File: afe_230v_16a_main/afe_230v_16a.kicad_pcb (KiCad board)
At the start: 2 copper layers, 342.7 x 117.6 mm, 60 parts, among them J4 MCV 1,5/ 6-G-3,81, J5 HBUS16, J6 pinheader_1x6, U2 AD8538, U3 AD8538_dnp, U4 AQH3223A, U5 ACS711xLCTR-25AB, U6 AD8538_dnp, U7 REF3030, U9 YAAJ_BlackPill

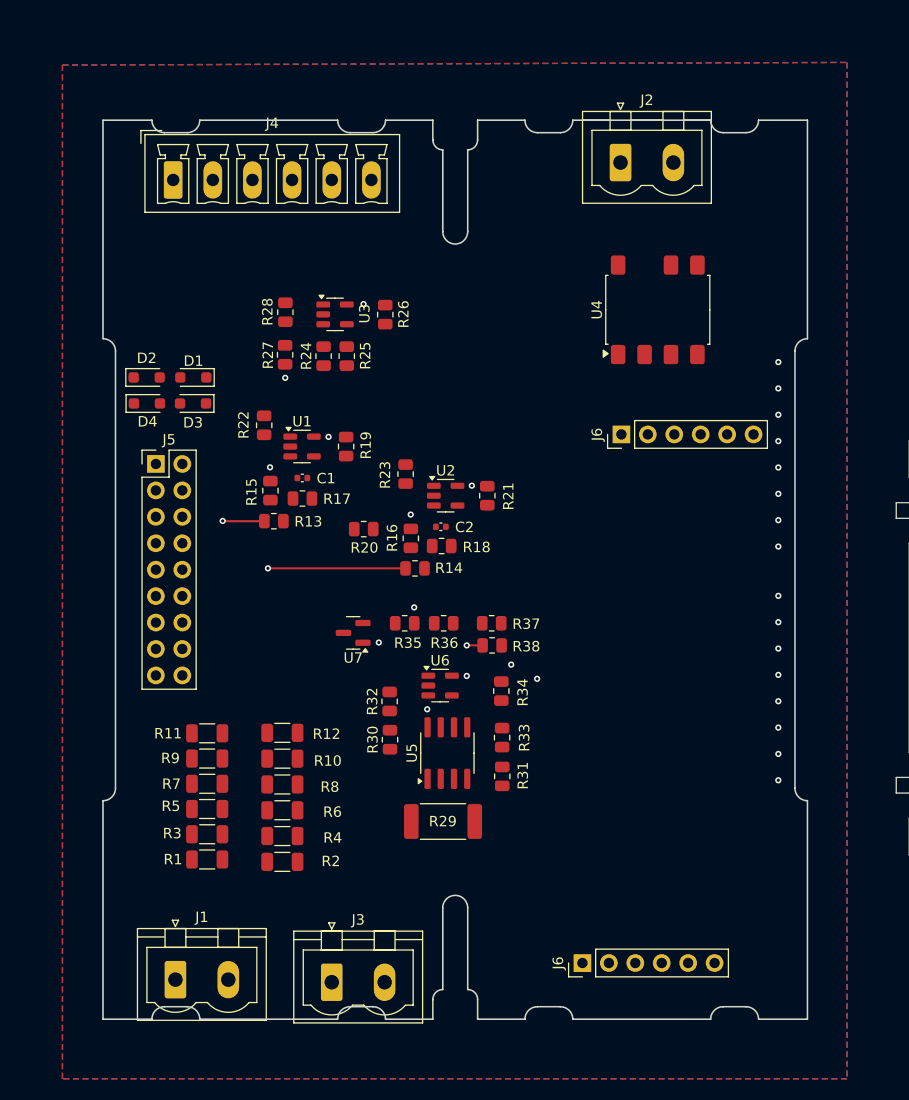
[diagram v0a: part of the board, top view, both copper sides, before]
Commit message: adjusted HBUS, DNP, & fixed A5toA2
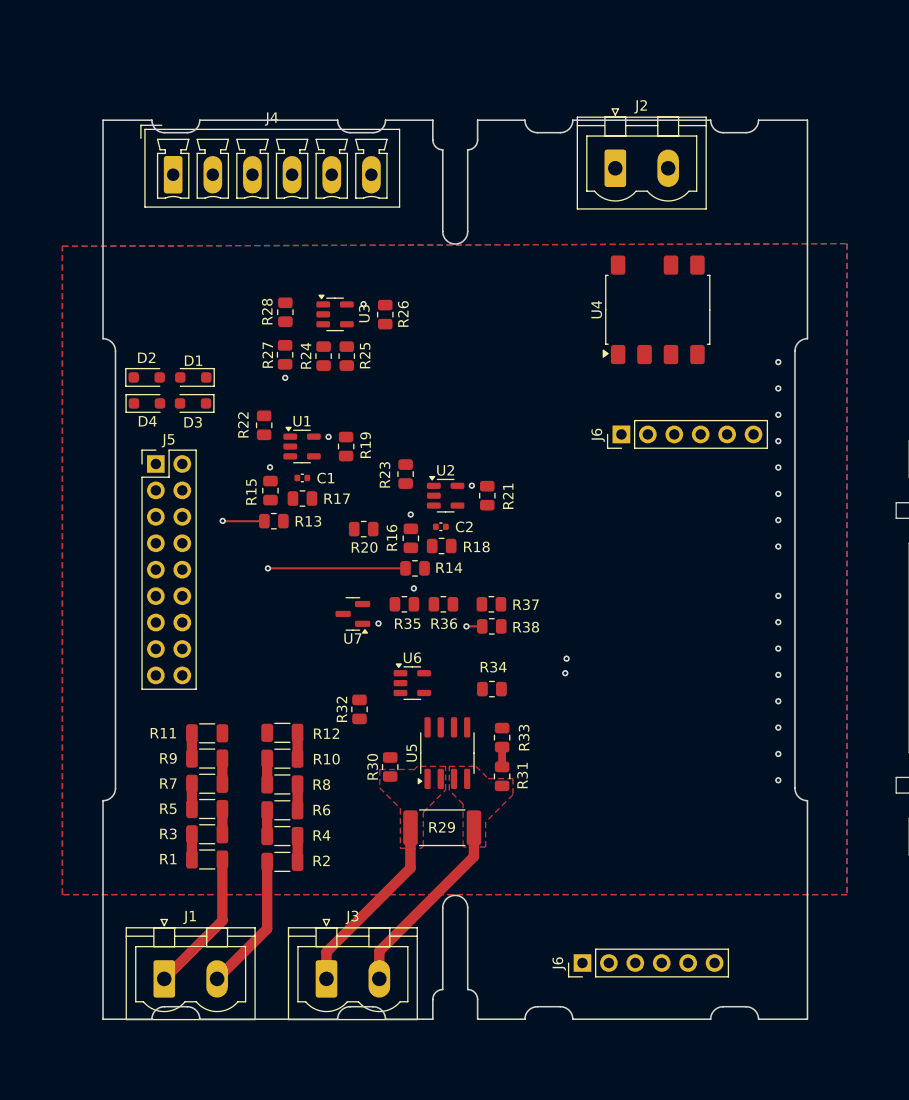
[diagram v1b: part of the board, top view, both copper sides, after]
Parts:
- moved R32 2.99 mm to (142.6, 108.1)
- moved U6 2.68 mm to (147.7, 105.5)
- moved R30 2.63 mm to (145.6, 113.6)
- moved R35 1.83 mm to (146.9, 98.0)
- moved R36 1.83 mm to (150.7, 98.0)
- moved R37 1.83 mm to (155.3, 98.0)
- moved R38 1.83 mm to (155.3, 100.1)
- moved U7 1.83 mm to (142.0, 98.9)
- moved J1 1.08 mm to (123.8, 134.0)
- moved R34 0.92 mm to (155.3, 106.1), turned to 180 degrees
- moved J2 0.74 mm to (167.2, 56.1)
- moved R29 0.61 mm to (150.6, 119.5)
- moved J3 0.60 mm to (139.4, 134.0)
- moved J4 0.50 mm to (124.7, 56.7)
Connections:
- J5 pad 1: /V0_sense -> /24V
- J5 pad 10: unconnected-(J5-Pin_10-Pad10) -> /V2_sense
- J5 pad 11: /CAN_hi -> /CAN_lo
- J5 pad 12: /K1_on -> /V3_sense
- J5 pad 13: /CAN_lo -> /I0_sense
- J5 pad 14: /K1_status -> /V4_sense
- J5 pad 15: /24V -> unconnected-(J5-Pin_15-Pad15)
- J5 pad 16: /K2_on -> unconnected-(J5-Pin_16-Pad16)
- J5 pad 17: /DGND -> unconnected-(J5-Pin_17-Pad17)
- J5 pad 18: /K2_status -> unconnected-(J5-Pin_18-Pad18)
- J5 pad 2: /V2_sense -> /K0_on
- J5 pad 3: /V1_sense -> /DGND
- J5 pad 4: /V3_sense -> /K1_on
- J5 pad 5: /K0_on -> /V0_sense
- J5 pad 6: /V4_sense -> /K0_status
- J5 pad 7: /K0_status -> /V1_sense
- J5 pad 8: /I0_sense -> /K1_status
- J5 pad 9: unconnected-(J5-Pin_9-Pad9) -> /CAN_hi
- U5 pad 7: /A5 -> /A2
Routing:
- net /I_n: track 0.00 -> 18.3 mm
- net /I_p: track 0.00 -> 17.9 mm
- net /V0_p: track 0.00 -> 13.8 mm
- net /V0_n: track 0.00 -> 13.2 mm
- net Net-(R4-Pad2): track 0.00 -> 2.48 mm
- net Net-(R2-Pad2): track 0.00 -> 2.48 mm
- net Net-(R10-Pad2): track 0.00 -> 2.48 mm
- net Net-(R10-Pad1): track 0.00 -> 2.48 mm
- net Net-(R6-Pad2): track 0.00 -> 2.48 mm
- net Net-(R5-Pad2): track 0.00 -> 2.43 mm
- net Net-(R7-Pad2): track 0.00 -> 2.42 mm
- net Net-(R3-Pad2): track 0.00 -> 2.42 mm
- net Net-(R11-Pad1): track 0.00 -> 2.42 mm
- net Net-(R1-Pad2): track 0.00 -> 2.42 mm
- net Net-(U6--): track 0.00 -> 1.90 mm
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- added copper zone on F.Cu, net /I_n
- added copper zone on F.Cu, net /I_p

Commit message: initial routing
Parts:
- moved J2 77.9 mm to (167.1, 134.0)
- moved J6 75.8 mm to (163.3, 56.6)
- moved U4 50.1 mm to (170.2, 119.8), turned to 180 degrees
- moved U6 4.70 mm to (143.4, 107.5)
- moved R32 3.68 mm to (143.4, 111.7)
- moved U7 0.52 mm to (142.0, 99.4)
- moved R34 0.15 mm to (155.4, 106.2)
- moved U5 0.09 mm to (151.0, 112.2)
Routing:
- net /3V3: track 0.00 -> 171.5 mm
- net /A2: track 0.00 -> 122.0 mm
- net /D0: track 0.00 -> 121.2 mm
- net /DGND: track 0.00 -> 103.2 mm
- net /A0: track 0.00 -> 102.4 mm, vias 0 -> 1
- net /A1: track 0.00 -> 96.9 mm, vias 0 -> 1
- net /V1_sense: track 13.2 -> 56.2 mm, vias 1 -> 2
- net /V0_sense: track 4.02 -> 45.2 mm, vias 1 -> 2
- net /1V5_REF: track 0.00 -> 39.7 mm
- net /I0_sense: track 1.53 -> 33.0 mm
- net /3V0_REF: track 0.00 -> 30.7 mm
- net Net-(R20-Pad2): track 0.00 -> 28.4 mm
- net Net-(R33-Pad2): track 0.00 -> 22.0 mm
- net /K_o: track 0.00 -> 18.5 mm
- net Net-(U6--): track 1.90 -> 16.8 mm
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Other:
- board text added: "DG 3v3 A0 A1 A2 D0"
- board text added: "I P"
- board text added: "K I"
- board text added: "K O"
- board text added: "V P"

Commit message: located daughterboard & updated connector
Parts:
- added 000: 0, Resistor_SMD:R_0805_2012Metric, F.Cu at (122.5, 72.3)
- added R39: 0, Resistor_SMD:R_0805_2012Metric, F.Cu at (1.71, 0.97)
- J6 (x2): value pinheader_1x6 -> pinheader_2x6_socket; footprint Connector_PinHeader_2.54mm:PinHeader_1x06_P2.54mm_Vertical -> Connector_PinHeader_2.54mm:PinHeader_2x06_P2.54mm_Vertical
- moved J6 4.47 mm to (245.5, 88.8)
- moved R1 2.63 mm to (125.7, 123.9), turned to 0 degrees
- moved R10 2.60 mm to (133.4, 111.0), turned to 90 degrees
- moved R12 2.58 mm to (136.0, 107.9), turned to 90 degrees
- moved J6 2.54 mm to (167.8, 84.2)
- moved R3 2.30 mm to (129.3, 121.9), turned to 90 degrees
- moved R6 1.74 mm to (133.6, 117.2), turned to 90 degrees
- moved R11 1.70 mm to (129.4, 109.5), turned to 90 degrees
- moved R5 1.59 mm to (126.9, 118.8), turned to 90 degrees
- moved U9 1.58 mm to (208.8, 113.6)
- moved R7 1.49 mm to (129.4, 115.7), turned to 90 degrees
- moved R2 1.45 mm to (134.5, 124.0)
- moved R8 1.40 mm to (136.0, 114.1), turned to 90 degrees
- moved R9 1.06 mm to (126.9, 112.6), turned to 90 degrees
- moved R4 0.88 mm to (136.1, 120.4), turned to 90 degrees
- renumbered J6 to J8
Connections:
- J6 pad 1: /DGND -> Earth (x2)
- J6 pad 2: /3V3 -> /DGND (x2)
- J6 pad 3: /A0 -> unconnected-(J6-Pin_3-Pad3) (x2)
- J6 pad 4: /A1 -> /3V3 (x2)
- J6 pad 5: /A2 -> unconnected-(J6-Pin_5-Pad5) (x2)
- J6 pad 6: /D0 -> /A0 (x2)
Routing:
- net /D0: track 121.2 -> 172.3 mm
- net /A2: track 122.0 -> 153.7 mm
- net /3V3: track 171.5 -> 202.8 mm
- net /A1: track 96.9 -> 124.0 mm
- net /A0: track 102.4 -> 125.0 mm
- net /V1_sense: track 56.2 -> 52.2 mm
- net /V0_p: track 13.8 -> 10.3 mm
- net /DGND: track 103.2 -> 106.3 mm, vias 0 -> 1
- net Net-(R4-Pad2): track 2.48 -> 0.00 mm
- net Net-(R2-Pad2): track 2.48 -> 0.00 mm
- net Net-(R10-Pad2): track 2.48 -> 0.00 mm
- net Net-(R10-Pad1): track 2.48 -> 0.00 mm
- net Net-(R6-Pad2): track 2.48 -> 0.00 mm
- net Net-(R5-Pad2): track 2.43 -> 0.00 mm
- net Net-(R7-Pad2): track 2.42 -> 0.00 mm
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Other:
- board size 342.7 x 117.6 mm -> 429.1 x 163.3 mm
- board text added: "BC 71,6 UT11/22 pcb4 13.6mm clearance"

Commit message: changed BP footprint, added stlink connection, added 3d models
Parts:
- removed U9: YAAJ_BlackPill, STM-32:YAAJ_BlackPill_SWD_2
- added C10: 0.1uF, Capacitor_SMD:C_0603_1608Metric_Pad1.08x0.95mm_HandSolder, F.Cu at (138.1, 67.5)
- added C4: 0.1uF, Capacitor_SMD:C_0603_1608Metric_Pad1.08x0.95mm_HandSolder, F.Cu at (143.6, 104.6)
- added C5: 0.1uF, Capacitor_SMD:C_0603_1608Metric_Pad1.08x0.95mm_HandSolder, F.Cu at (151.0, 83.6)
- added C6: 0.1uF, Capacitor_SMD:C_0603_1608Metric_Pad1.08x0.95mm_HandSolder, F.Cu at (136.4, 78.8)
- added J7: 1x02_pinheader, Connector_PinHeader_2.54mm:PinHeader_1x02_P2.54mm_Vertical, F.Cu at (157.8, 57.9)
- added J9: Conn_01x04_STlink_pinheader, Connector_PinHeader_2.54mm:PinHeader_1x04_P2.54mm_Vertical, F.Cu at (173.3, 132.9)
- added U10: BlackPill_F4_SWI, MSZ_STM32:Blackpill_F4_SWI, F.Cu at (208.0, 112.1)
- J8: value pinheader_1x6 -> 1x06_pinheader
- moved J2 8.19 mm to (159.0, 134.5)
- moved J1 5.88 mm to (129.7, 133.7), turned to 180 degrees
- moved J3 5.06 mm to (144.5, 133.7), turned to 180 degrees
- moved J4 0.50 mm to (124.7, 56.2)
- moved R29 0.48 mm to (151.0, 119.3)
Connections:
- J6 pad 11: unconnected-(J6-Pin_11-Pad11) -> /3V3 (x2)
- J6 pad 3: unconnected-(J6-Pin_3-Pad3) -> /5v (x2)
- J6 pad 7: unconnected-(J6-Pin_7-Pad7) -> /SCK (x2)
- J6 pad 9: unconnected-(J6-Pin_9-Pad9) -> /DIO (x2)
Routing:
- net /5v: track 0.00 -> 131.0 mm, vias 0 -> 2
- net /3V3: track 202.8 -> 318.5 mm, vias 4 -> 7
- net /DIO: track 0.00 -> 70.0 mm
- net /SCK: track 0.00 -> 69.1 mm
- net Earth: track 0.00 -> 49.5 mm, vias 57 -> 106
- net /I_n: track 18.3 -> 0.00 mm, vias 0 -> 3
- net /I_p: track 17.9 -> 0.00 mm, vias 0 -> 3
- net /K_o: track 18.5 -> 0.70 mm
- net /V0_n: track 11.7 -> 0.00 mm
- net /K_i: track 10.9 -> 0.00 mm
- net /V0_p: track 10.3 -> 0.00 mm
- net /DGND: track 106.3 -> 110.5 mm
- net /A1: track 124.0 -> 122.3 mm
- net /A2: track 153.7 -> 152.0 mm
- net /D0: track 172.3 -> 171.3 mm
- added copper zone on B.Cu, net /I_n
- added copper zone on B.Cu, net /I_p
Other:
- board size 429.1 x 163.3 mm -> 146 x 86.4 mm
- board text added: "DG 5V"
- board text added: "ST-Link"
- board text added: "fix these"
- board text removed: "pcb2 BC71,6 UT-11' 3,55 clearance"
- board text removed: "pcb3 BC71,6 UT-11' 8,6 clearance"

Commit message: swapped connectors
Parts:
- removed 000: 0, Resistor_SMD:R_0805_2012Metric
- removed J3: ~, Connector_Phoenix_MSTB:PhoenixContact_MSTBVA_2,5_2-G-5,08_1x02_P5.08mm_Vertical
- removed J4: MCV 1,5/ 6-G-3,81, Connector_Phoenix_MC:PhoenixContact_MCV_1,5_6-G-3.81_1x06_P3.81mm_Vertical
- removed J7: 1x02_pinheader, Connector_PinHeader_2.54mm:PinHeader_1x02_P2.54mm_Vertical
- removed J8: 1x06_pinheader, Connector_PinHeader_2.54mm:PinHeader_1x06_P2.54mm_Vertical
- added D5: LED, LED_SMD:LED_0805_2012Metric, F.Cu at (234.2, 87.8)
- added D6: LED, LED_SMD:LED_0805_2012Metric, F.Cu at (236.6, 85.8)
- added J6: pinheader_2x6_socket, Connector_PinHeader_2.54mm:PinHeader_2x06_P2.54mm_Vertical, F.Cu at (162.9, 58.7)
- added R40: 2.2k, Resistor_SMD:R_0805_2012Metric, F.Cu at (231.0, 87.0)
- added R41: 2.2k, Resistor_SMD:R_0805_2012Metric, F.Cu at (230.9, 84.8)
- J1: value ~ -> MKDSN 2,5/ 6-5,08; footprint Connector_Phoenix_MSTB:PhoenixContact_MSTBVA_2,5_2-G-5,08_1x02_P5.08mm_Vertical -> kyuditsky:1989405
- J2: value ~ -> MKDS 1,5/ 6; footprint Connector_Phoenix_MSTB:PhoenixContact_MSTBVA_2,5_2-G-5,08_1x02_P5.08mm_Vertical -> kyuditsky:1715190
- moved R39 139.7 mm to (123.2, 70.1), turned to -90 degrees
- moved J2 87.7 mm to (121.3, 55.3)
- moved J1 8.58 mm to (121.1, 134.3), turned to 0 degrees
- moved R32 2.84 mm to (140.9, 110.3), turned to 180 degrees
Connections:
- J2 pad 1: /K_i -> /DGND
- J2 pad 2: /K_o -> /3V3
- J6 pad 5: unconnected-(J6-Pin_5-Pad5) -> /DGND (x2)
- J9 pad 1: Earth -> /DGND
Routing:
- net /3V3: track 318.5 -> 380.8 mm, vias 7 -> 8
- net /DGND: track 110.5 -> 168.0 mm
- net /K_i: track 0.00 -> 40.1 mm, vias 0 -> 1
- net /K_o: track 0.70 -> 40.3 mm, vias 0 -> 1
- net /DIO: track 70.0 -> 105.4 mm, vias 0 -> 1
- net /SCK: track 69.1 -> 104.3 mm, vias 0 -> 1
- net /V0_n: track 0.00 -> 13.1 mm
- net /V0_p: track 0.00 -> 11.7 mm
- net /5v: track 131.0 -> 135.9 mm
- net Net-(D6-K): track 0.00 -> 4.79 mm
- net /A1: track 122.3 -> 125.4 mm
- net /A0: track 124.8 -> 127.1 mm
- net Net-(D5-K): track 0.00 -> 2.17 mm
- net Net-(U6--): track 16.8 -> 15.7 mm
- net Net-(R33-Pad2): track 22.0 -> 21.1 mm
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- removed copper zone on B.Cu, net /I_n
- removed copper zone on B.Cu, net /I_p
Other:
- outline, holes or cut-outs redrawn
- board text added: "3v3"
- board text added: "5v"
- board text added: "DG 5v"
- board text added: "afe_230v_16a rev.01 jan25 //keyudits"
- board text removed: "DG 5V"
- board text removed: "I P"
- board text removed: "K I"
- board text removed: "K O"
- board text removed: "V P"
- board text removed: "fix these"
